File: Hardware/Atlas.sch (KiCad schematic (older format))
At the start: 28 parts

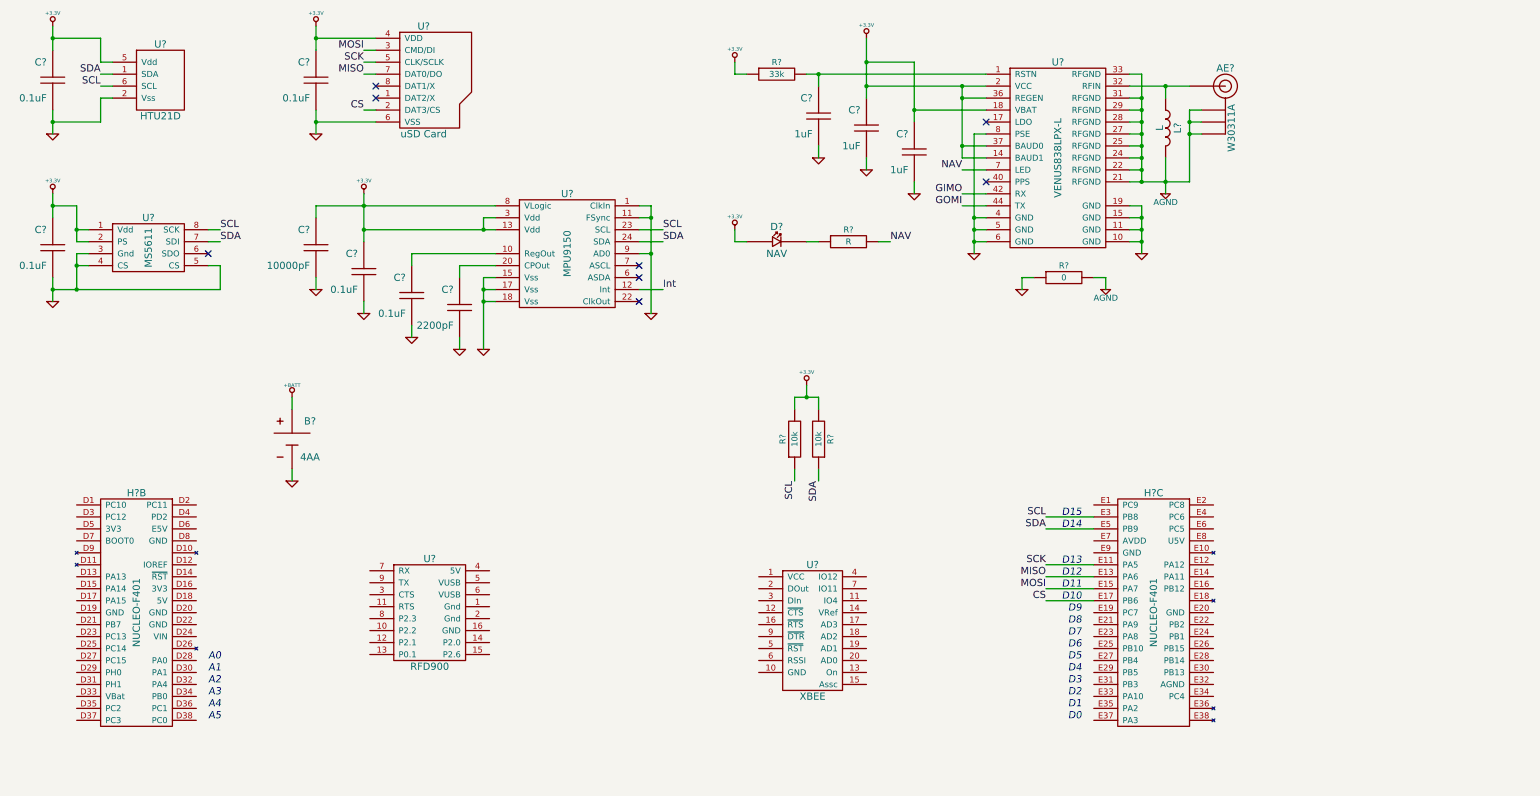
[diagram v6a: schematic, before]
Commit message: Radio support components
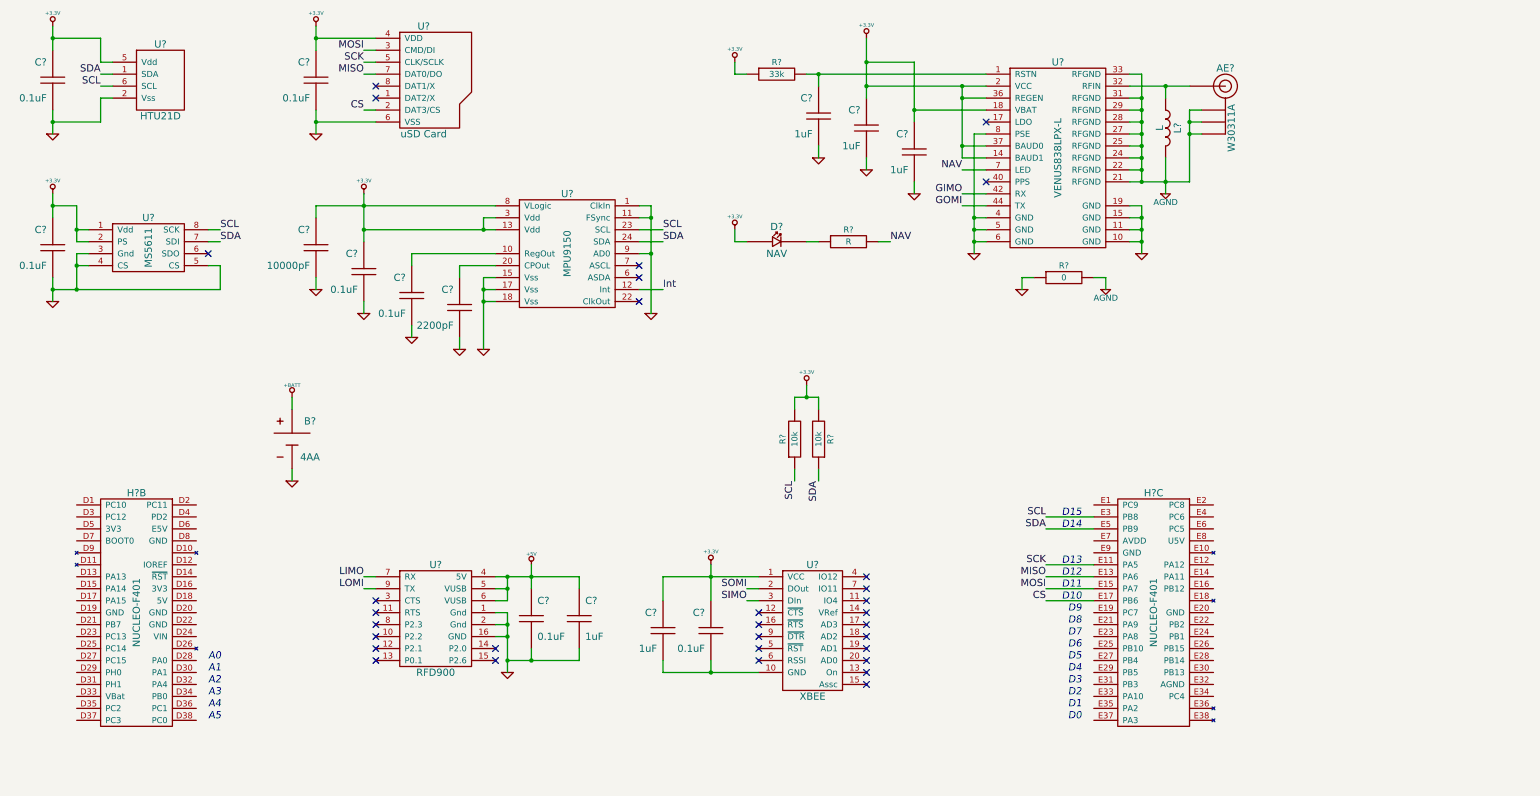
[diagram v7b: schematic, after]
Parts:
- added C? (x2): 0.1uF, CAPC1608-N, symbol C
- added C? (x2): 1uF, CAPC1608-N, symbol C
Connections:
- net +3.3V: now also U?.1 (VCC), C?.1, C?.1
- net GND: now also U?.1 (Gnd), U?.16 (GND), U?.2 (Gnd), C?.2, C?.2
- net +5V: now reaches U?.4 (5V)
- net +5V: now also U?.5 (VUSB), U?.6 (VUSB), C?.1, C?.1
- net LIMO: now reaches U?.7 (RX)
- net LOMI: now reaches U?.9 (TX)
- net at U?.10 (GND): now also C?.2, C?.2
- net SOMI: now reaches U?.2 (DOut)
- net SIMO: now reaches U?.3 (DIn)
- no-connect marks 8 -> 31
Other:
- moved on the sheet: U?

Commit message: Rough netlist, association and layout
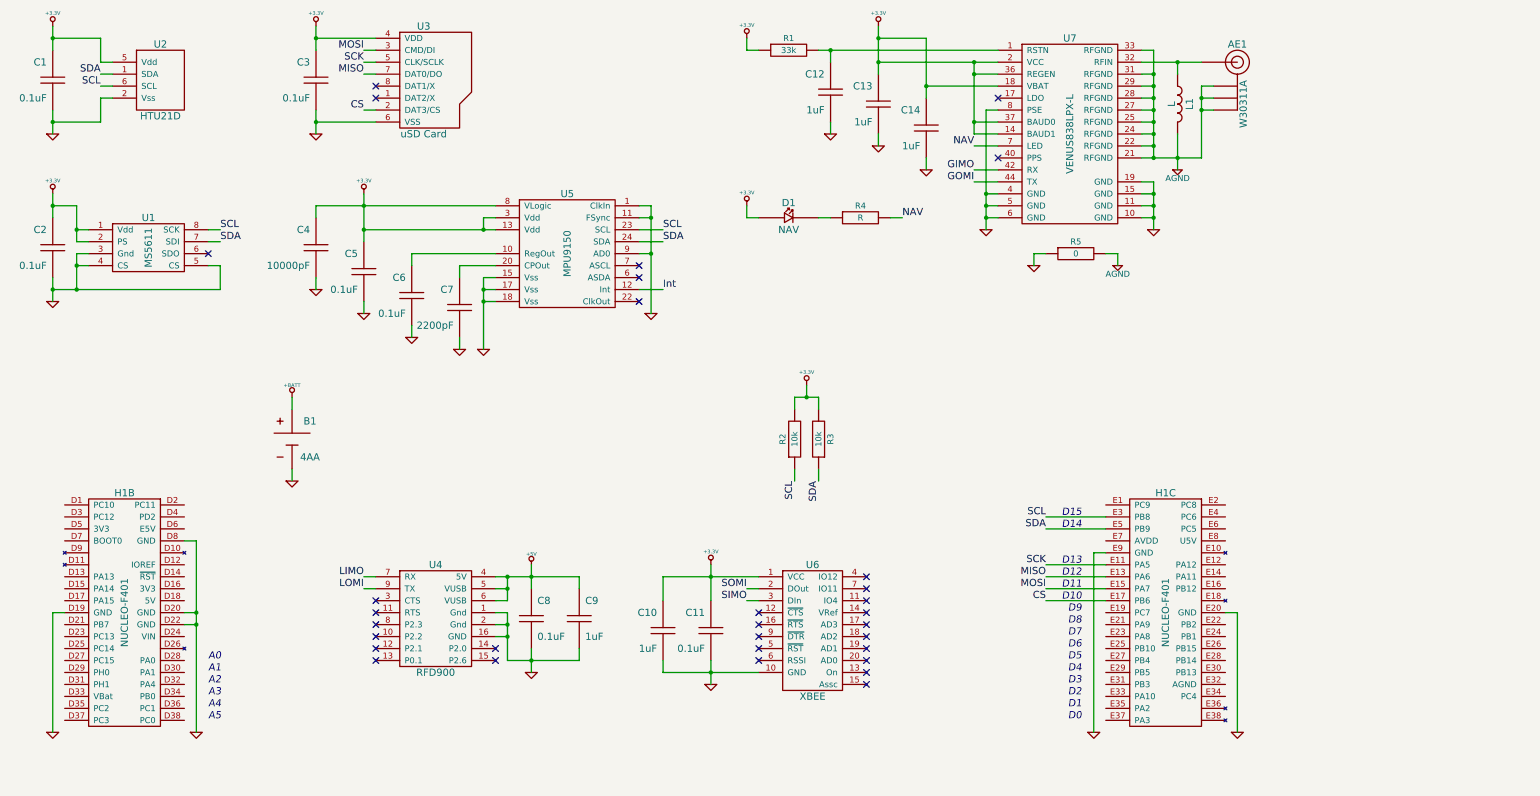
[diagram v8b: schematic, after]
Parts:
- gave numbers to parts that had none: 31
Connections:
- net GND: now also C10.2, C11.2, H1.D19 (GND), H1.D20 (GND), H1.D22 (GND), H1.D8 (GND), H1.E20 (GND), H1.E9 (GND), U6.10 (GND)
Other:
- moved on the sheet: AE1, C12, C13, C14, D1, H1B, H1C, L1, R1, R4, R5, U7
